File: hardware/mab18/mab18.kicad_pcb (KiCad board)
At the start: 2 copper layers, 114.5 x 140 mm, 86 parts, among them J101 PUMP_1 _OUT, J102 PUMP_1_IN, J103 PUMP_1 _OUT, J104 PUMP_2_IN, J105 PUMP_3_OUT, J106 PUMP_3_IN, J107 BATTERY, K101 coil: 12VDC, contact: 125V/10A, K102 coil: 12VDC, contact: 125V/10A, K103 coil: 12VDC, contact: 125V/10A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

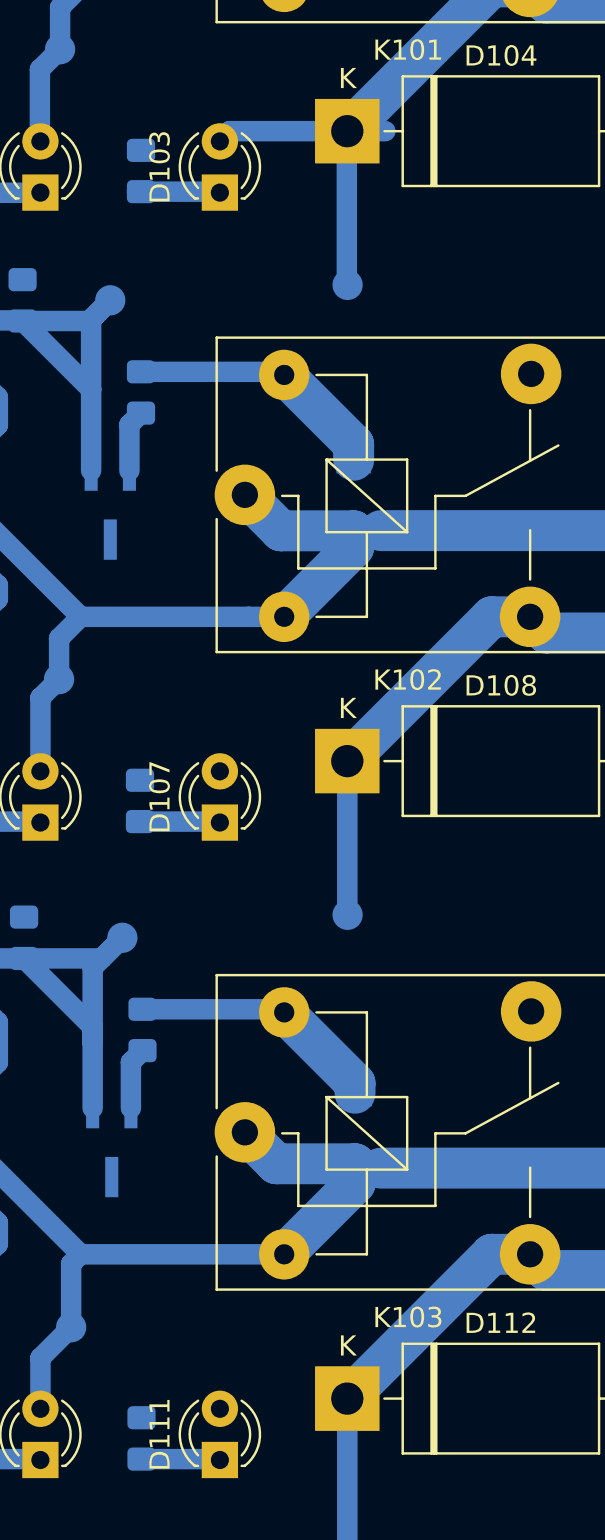
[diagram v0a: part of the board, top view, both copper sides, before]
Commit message: PCB Stack changed. PCB DRC OK.
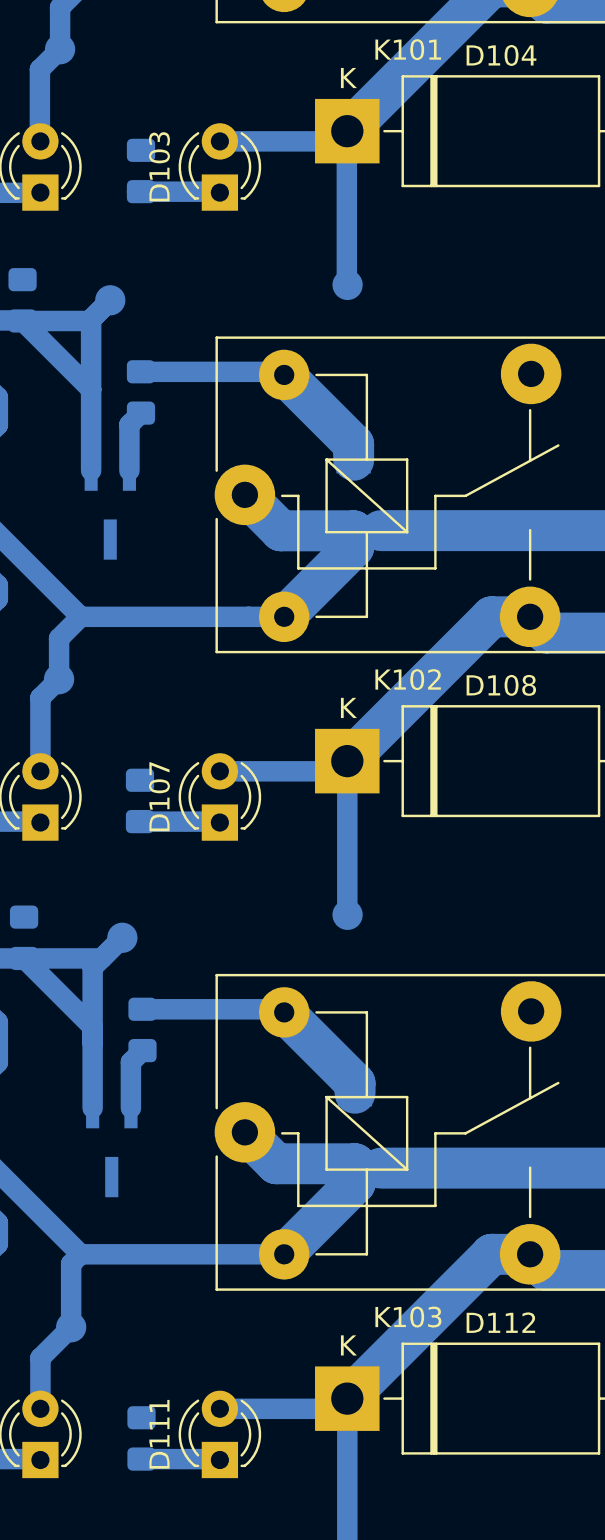
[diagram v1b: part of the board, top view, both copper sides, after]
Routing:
- net Net-(D111-Pad2): track 60.2 -> 66.7 mm
- net Net-(D107-Pad2): track 60.2 -> 66.7 mm
- net Net-(D103-Pad2): track 109.2 -> 107.3 mm
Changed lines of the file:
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@@
     (thickness 1.6)
     (drawings 4)
-    (tracks 271)
+    (tracks 274)
     (zones 0)
     (modules 86)
@@
   (page A4)
   (layers
-    (0 F.Cu signal)
+    (0 F.Cu jumper)
     (31 B.Cu signal)
     (32 B.Adhes user)
+    (33 F.Adhes user)
     (34 B.Paste user)
+    (35 F.Paste user)
     (36 B.SilkS user)
+    (37 F.SilkS user)
     (38 B.Mask user)
+    (39 F.Mask user)
     (40 Dwgs.User user)
     (41 Cmts.User user)
@@
     (47 F.CrtYd user)
     (48 B.Fab user)
+    (49 F.Fab user)
   )
   (setup
@@
   (gr_line (start 676 12.5) (end 676 -127.5) (layer Edge.Cuts) (width 0.15))
   (gr_line (start 561.5 12.5) (end 676 12.5) (layer Edge.Cuts) (width 0.15))
-  (segment (start 612.496 -63.201) (end 611.989 -62.694) (width 1.016) (layer B.Cu) (net 1))
-  (segment (start 618.31 -63.201) (end 612.496 -63.201) (width 1.016) (layer B.Cu) (net 1))
-  (segment (start 620.222 -63.201) (end 618.31 -63.201) (width 1.016) (layer B.Cu) (net 1))
   (segment (start 618.31 -55.61) (end 618.275 -55.575) (width 1.016) (layer B.Cu) (net 1))
   (segment (start 618.31 -63.201) (end 618.31 -55.61) (width 1.016) (layer B.Cu) (net 1))
@@
   (segment (start 625.493 -70.359) (end 618.335 -63.201) (width 2.032) (layer B.Cu) (net 1))
   (segment (start 627.405 -70.359) (end 625.493 -70.359) (width 2.032) (layer B.Cu) (net 1))
+  (segment (start 617.828 -62.694) (end 618.335 -63.201) (width 1.016) (layer B.Cu) (net 1))
+  (segment (start 612.014 -62.694) (end 617.828 -62.694) (width 1.016) (layer B.Cu) (net 1))
   (segment (start 585.543 -44.651) (end 588.109 -44.651) (width 1.016) (layer B.Cu) (net 2))
   (segment (start 582.999 -44.651) (end 585.543 -44.651) (width 1.016) (layer B.Cu) (net 2))
@@
   (segment (start 628.209 -6.68) (end 627.405 -7.484) (width 2.032) (layer B.Cu) (net 7))
   (segment (start 667.6 -6.68) (end 628.209 -6.68) (width 2.032) (layer B.Cu) (net 7))
+  (segment (start 617.828 0.181) (end 618.335 -0.326) (width 1.016) (layer B.Cu) (net 7))
+  (segment (start 612.014 0.181) (end 617.828 0.181) (width 1.016) (layer B.Cu) (net 7))
   (segment (start 618.933 -11.76) (end 618.718 -11.975) (width 1.016) (layer B.Cu) (net 8))
   (segment (start 605.107 -7.484) (end 615.205 -7.484) (width 1.016) (layer B.Cu) (net 8))
@@
   (segment (start 628.209 -38.305) (end 627.405 -39.109) (width 2.032) (layer B.Cu) (net 10))
   (segment (start 667.6 -38.305) (end 628.209 -38.305) (width 2.032) (layer B.Cu) (net 10))
+  (segment (start 617.828 -31.444) (end 618.335 -31.951) (width 1.016) (layer B.Cu) (net 10))
+  (segment (start 612.014 -31.444) (end 617.828 -31.444) (width 1.016) (layer B.Cu) (net 10))
   (segment (start 613.437234 -39.109) (end 615.205 -39.109) (width 1.016) (layer B.Cu) (net 11))
   (segment (start 605.107 -39.109) (end 613.437234 -39.109) (width 1.016) (layer B.Cu) (net 11))
